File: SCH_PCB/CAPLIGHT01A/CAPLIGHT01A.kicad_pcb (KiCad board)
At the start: 2 copper layers, 59.7 x 20.3 mm, 29 parts, among them J1 JUMP_3X2, J10 JUMP_2x1, J11 JUMP_3X2, J13 CONN_2, J2 CONN1_1, J3 CONN1_1, J4 CONN1_1, J5 CONN1_1, J6 CONN1_1, J7 CONN1_1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

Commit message: nová verze
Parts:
- C3: moved to B.Cu
- moved C3 6.35 mm to (201.9, 121.9)
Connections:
- D2 pad 1: GND -> Net-(C2-Pad2)
- R7 pad 1: Net-(C2-Pad1) -> (no net)
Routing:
- net Net-(C2-Pad2): track 45.1 -> 83.9 mm, vias 0 -> 1
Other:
- board size 59.7 x 20.3 mm -> 73.7 x 20.3 mm

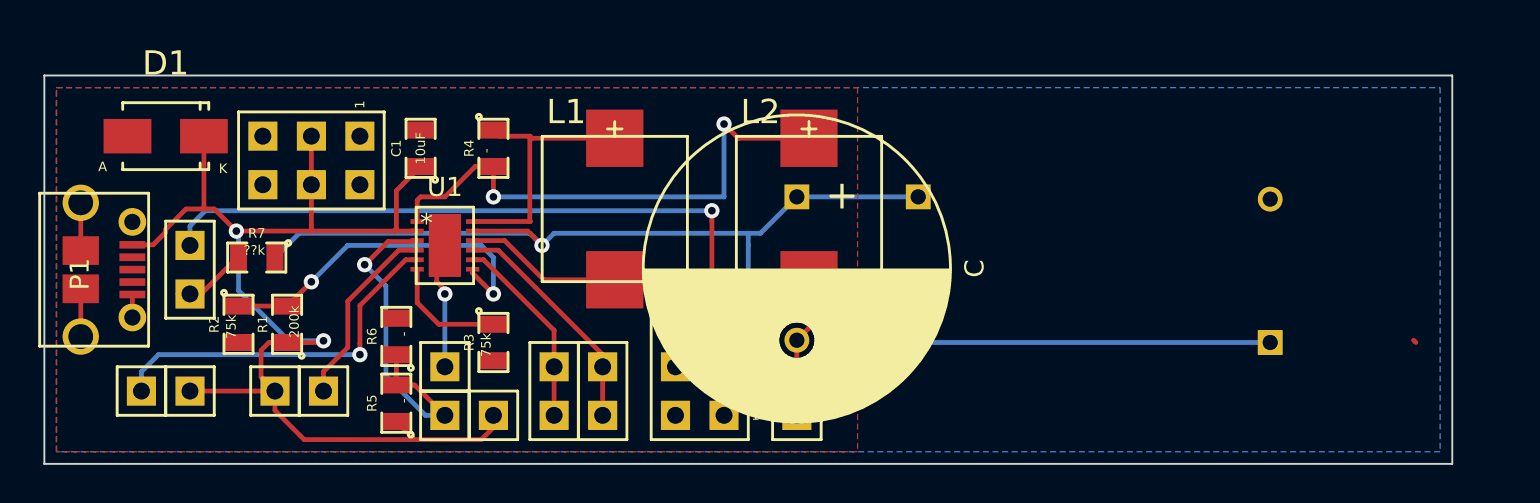
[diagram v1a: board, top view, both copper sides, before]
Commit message: Second capacitor SMD pad
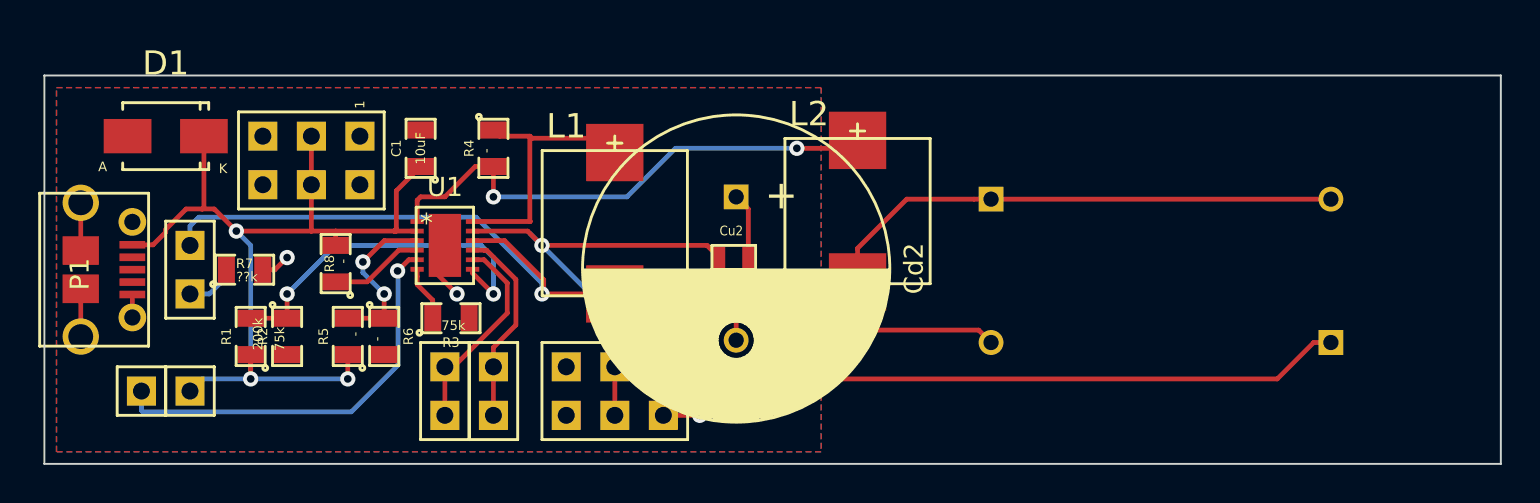
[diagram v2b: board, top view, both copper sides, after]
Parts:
- removed C: C, Mlab_C:C_Radial_D16_L25_P7.5
- removed C2, C3: 22F, Mlab_C:C_Radial_D16_L25_P7.5
- removed J13: CONN_2, Mlab_Pin_Headers:Straight_1x01
- removed J2, J3, J4, J7, J8: CONN1_1, Mlab_Pin_Headers:Straight_1x01
- added Cd1: 22F, Mlab_C:C_Radial_D16_L25_P7.5, B.Cu at (187.3, 114.4)
- added Cd2: 22F, Mlab_C:C_Radial_D16_L25_P7.5, F.Cu at (174.0, 114.3)
- added Cu1: 22F, Mlab_C:C_Radial_D16_L25_P7.5, B.Cu at (205.1, 121.9)
- added Cu2: 100uF, Mlab_C:SMD-0603, F.Cu at (173.9, 117.5)
- added R8: -, Mlab_R:SMD-0805, F.Cu at (153.0, 117.8)
- moved J10 5.72 mm to (161.3, 124.5), turned to 270 degrees
- moved J9 5.72 mm to (158.8, 124.5)
- moved J11 4.62 mm to (167.6, 124.5), turned to 270 degrees
- moved J5 4.45 mm to (145.4, 124.5)
- moved R5 4.32 mm to (153.7, 121.6)
- moved R2 2.62 mm to (150.5, 121.6)
- moved R3 2.56 mm to (159.1, 120.7), turned to 0 degrees
- moved L2 2.54 mm to (180.3, 115.0)
- moved R1 2.01 mm to (148.6, 121.6)
- moved R7 0.90 mm to (148.3, 118.1), turned to 0 degrees
- moved L1 0.75 mm to (167.6, 115.7)
- moved R6 0.64 mm to (155.6, 121.6), turned to 270 degrees
- turned D2 to 180 degrees
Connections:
- net /CTL renamed Net-(R5-Pad2)
- D2 pad 1: Net-(C2-Pad2) -> Net-(D2-Pad1)
- D2 pad 2: Net-(D2-Pad2) -> Net-(Cd1-Pad1)
- L1 pad 2: Net-(C2-Pad2) -> Net-(Cd1-Pad1)
- L2 pad 2: Net-(C2-Pad2) -> Net-(Cd1-Pad1)
- R7 pad 1: (no net) -> Net-(D2-Pad1)
- R7 pad 2: Net-(D2-Pad2) -> GND
- U1 pad 10: Net-(C2-Pad2) -> Net-(Cd1-Pad1)
- U1 pad 4: /VSEL -> Net-(R8-Pad1)
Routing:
- net Net-(C2-Pad2): track 83.9 -> 0.00 mm, vias 1 -> 0
- net Net-(Cd1-Pad1): track 0.00 -> 76.0 mm, vias 0 -> 1
- net GND: track 11.9 -> 29.8 mm, vias 1 -> 7
- net Net-(Cu1-Pad1): track 50.2 -> 65.7 mm, vias 1 -> 2
- net /VIN: track 63.8 -> 49.0 mm, vias 2 -> 3
- net /VSEL: track 9.96 -> 0.00 mm
- net Net-(R5-Pad2): track 18.5 -> 8.82 mm, vias 1 -> 2
- net Net-(R8-Pad1): track 0.00 -> 4.95 mm
- net Net-(R3-Pad1): track 6.84 -> 2.90 mm
- net Net-(D2-Pad2): track 3.83 -> 0.00 mm
- net Net-(D2-Pad1): track 0.00 -> 2.65 mm
- net /EN: track 19.4 -> 21.7 mm
- net /PG: track 12.2 -> 10.5 mm
- net /#PFO: track 10.2 -> 10.9 mm
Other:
- board size 73.7 x 20.3 mm -> 76.2 x 20.3 mm
- board text added: "#PFO"
- board text added: "EN"
- board text added: "PG"
- board text added: "VIN"
- board text added: "VOUT"

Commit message: pcb labels
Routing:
- net Net-(Cu1-Pad1): track 65.7 -> 64.7 mm
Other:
- net class Default: trace_width 0.25 -> 0.3
- rule via_min_size: 0.4 -> 0.7
- board text added: "LED"
- board text added: "OUT"
- board text added: "Power IN"
- board text removed: "VIN"
- board text removed: "VOUT"

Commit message: label
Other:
- board text added: "+"
- board text added: "2016"
- board text added: "CAPLIGHT01A"
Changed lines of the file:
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@@
   (general
     (links 66)
-    (no_connects 1)
-    (area 131.754999 86.207271 215.4975 131.135002)
+    (no_connects 0)
+    (area 137.744999 107.899999 214.045001 128.320001)
     (thickness 1.6)
-    (drawings 13)
-    (tracks 168)
+    (drawings 16)
+    (tracks 169)
     (zones 0)
     (modules 25)
@@
     )
   )
+  (gr_text + (at 176.53 114.3) (layer B.SilkS)
+    (effects (font (size 2 2) (thickness 0.3)) (justify mirror))
+  )
+  (gr_text 2016 (at 167.005 111.76) (layer B.SilkS)
+    (effects (font (size 1.3 1.3) (thickness 0.3)) (justify mirror))
+  )
+  (gr_text CAPLIGHT01A (at 167.64 109.855) (layer B.SilkS)
+    (effects (font (size 1.5 1.5) (thickness 0.35)) (justify mirror))
+  )
   (gr_line (start 178.435 107.95) (end 178.435 128.27) (layer B.SilkS) (width 0.2))
   (gr_text LED (at 148.59 118.11) (layer B.SilkS)
@@
     (effects (font (size 1.5 1.5) (thickness 0.3)) (justify mirror))
   )
-  (gr_text "Power IN\n" (at 151.765 109.22) (layer B.SilkS)
+  (gr_text "Power IN\n" (at 150.495 109.22) (layer B.SilkS)
     (effects (font (size 1.5 1.5) (thickness 0.3)) (justify mirror))
   )
@@
   (segment (start 157.3 118.8865) (end 157.3 118.465) (width 0.25) (layer F.Cu) (net 9))
   (segment (start 157.3 118.465) (end 157.3 118.09) (width 0.25) (layer F.Cu) (net 9))
-  (segment (start 147.32 118.487) (end 147.32 118.11) (width 0.25) (layer B.Cu) (net 10))
-  (segment (start 145.415 119.38) (end 146.427 119.38) (width 0.25) (layer B.Cu) (net 10))
-  (segment (start 146.427 119.38) (end 147.32 118.487) (width 0.25) (layer B.Cu) (net 10))
+  (segment (start 146.05 118.745) (end 146.05 118.6355) (width 0.3) (layer F.Cu) (net 10))
+  (segment (start 146.05 118.6355) (end 146.5755 118.11) (width 0.3) (layer F.Cu) (net 10))
+  (segment (start 146.5755 118.11) (end 147.32 118.11) (width 0.3) (layer F.Cu) (net 10))
+  (segment (start 145.415 119.38) (end 146.05 118.745) (width 0.3) (layer F.Cu) (net 10))
   (segment (start 187.325 114.42) (end 205.105 114.42) (width 0.25) (layer F.Cu) (net 11))
   (segment (start 180.34 118.745) (end 180.34 116.995) (width 0.25) (layer F.Cu) (net 11))

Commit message: only for ExpaLight
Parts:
- removed Cd1, Cd2, Cu1: 22F, Mlab_C:C_Radial_D16_L25_P7.5
- removed Cu2: 100uF, Mlab_C:SMD-0603
- removed J10, J9: JUMP_2x1, Mlab_Pin_Headers:Straight_2x01
- removed J11: JUMP_3X2, Mlab_Pin_Headers:Straight_2x03
- removed J5, J6: CONN1_1, Mlab_Pin_Headers:Straight_1x01
- removed L2: DER0705-3.3uH, Mlab_L:DER0705
- removed R6, R8: -, Mlab_R:SMD-0805
- removed R7: ??k, Mlab_R:SMD-0805
- added C2: 100uF, Mlab_C:TantalC_SizeC_Reflow, F.Cu at (156.9, 123.2)
- added C3: 22F, Mlab_C:C_Radial_D18_L25_P7.5, B.Cu at (168.3, 121.8)
- added J2: CONN1_1, Mlab_Pin_Headers:Straight_1x01, F.Cu at (150.5, 109.9)
- added J3: CONN1_1, Mlab_Pin_Headers:Straight_1x01, F.Cu at (150.5, 112.4)
- R1: value 200k -> -
- R2: value 75k -> 287k
- R3: value 75k -> 100k
- R4: value - -> 71.5k
- R5: value - -> ??k
- moved D1 14.1 mm to (142.3, 125.1)
- moved R1 11.4 mm to (153.7, 111.4)
- moved R4 11.1 mm to (150.8, 115.6), turned to 180 degrees
- moved R3 8.86 mm to (150.5, 118.4), turned to 90 degrees
- moved J1 7.10 mm to (144.8, 111.1), turned to 90 degrees
- moved R5 6.84 mm to (147.3, 124.1)
- moved L1 5.08 mm to (162.6, 115.7)
- moved U1 3.85 mm to (154.9, 117.0), turned to 270 degrees
- moved C1 1.31 mm to (156.2, 111.4), turned to 270 degrees
- moved D2 1.27 mm to (146.7, 118.1), turned to 0 degrees
- moved R2 0.63 mm to (150.5, 122.2), turned to 90 degrees
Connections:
- D2 pad 1: Net-(D2-Pad1) -> GND
- D2 pad 2: Net-(Cd1-Pad1) -> Net-(D2-Pad2)
- L1 pad 2: Net-(Cd1-Pad1) -> Net-(C2-Pad2)
- R1 pad 1: /VIN -> Net-(R1-Pad1)
- R1 pad 2: Net-(R1-Pad2) -> /VIN
- R2 pad 1: Net-(R1-Pad2) -> /VIN
- R2 pad 2: GND -> Net-(R2-Pad2)
- R3 pad 1: Net-(R3-Pad1) -> Net-(R2-Pad2)
- R4 pad 1: Net-(L1-Pad1) -> Net-(R4-Pad1)
- R4 pad 2: Net-(L2-Pad1) -> GND
- R5 pad 1: /VIN -> Net-(C2-Pad2)
- R5 pad 2: Net-(R5-Pad2) -> Net-(D2-Pad2)
- U1 pad 1: Net-(L2-Pad1) -> Net-(L1-Pad1)
- U1 pad 10: Net-(Cd1-Pad1) -> Net-(C2-Pad2)
- U1 pad 3: Net-(R5-Pad2) -> /VIN
- U1 pad 4: Net-(R8-Pad1) -> Net-(R1-Pad1)
- U1 pad 6: Net-(R3-Pad1) -> Net-(R4-Pad1)
- U1 pad 7: Net-(R1-Pad2) -> Net-(R2-Pad2)
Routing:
- net Net-(Cd1-Pad1): track 76.0 -> 0.00 mm, vias 1 -> 0
- net Net-(C2-Pad1): track 64.7 -> 6.25 mm, vias 2 -> 0
- net Net-(C2-Pad2): track 0.00 -> 33.0 mm
- net GND: track 29.8 -> 0.00 mm, vias 7 -> 5
- net Net-(L2-Pad1): track 27.7 -> 0.00 mm, vias 2 -> 0
- net Net-(R1-Pad2): track 18.9 -> 0.00 mm, vias 2 -> 0
- net /EN: track 21.7 -> 6.48 mm, vias 1 -> 0
- net /#PFO: track 10.9 -> 0.00 mm
- net /PG: track 10.5 -> 0.00 mm
- net Net-(R5-Pad2): track 8.82 -> 0.00 mm, vias 2 -> 0
- net Net-(R2-Pad2): track 0.00 -> 5.43 mm
- net Net-(R8-Pad1): track 4.95 -> 0.00 mm
- net Net-(D2-Pad2): track 0.00 -> 4.07 mm
- net Net-(R1-Pad1): track 0.00 -> 3.61 mm
- net Net-(R3-Pad1): track 2.90 -> 0.00 mm
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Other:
- board size 76.2 x 20.3 mm -> 33 x 20.3 mm
- board text removed: "#PFO"
- board text removed: "+"
- board text removed: "2016"
- board text removed: "CAPLIGHT01A"
- board text removed: "EN"
- board text removed: "LED"
- board text removed: "OUT"
- board text removed: "PG"
- board text removed: "Power IN"

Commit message: layout edit
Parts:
- J2: footprint Mlab_Pin_Headers:Straight_1x01 -> Measurement_Points:Measurement_Point_Round-SMD-Pad_Small
- J3: value CONN1_1 -> JUMP_2x1; footprint Mlab_Pin_Headers:Straight_1x01 -> Measurement_Points:Measurement_Point_Round-SMD-Pad_Small
- moved J3 8.64 mm to (153.0, 120.7), turned to 0 degrees
- moved J2 2.54 mm to (150.5, 112.4)
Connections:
- J2 pad 1: /VIN -> /EN
- J3 pad 1: /EN -> /#PFO
- U1 pad 9: /PG -> (no net)
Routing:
- net GND: track 0.00 -> 7.32 mm, vias 5 -> 0
- net Net-(L1-Pad1): track 11.9 -> 17.6 mm, vias 0 -> 4
- net /#PFO: track 0.00 -> 2.81 mm
- net /VIN: track 47.0 -> 45.4 mm
- net /EN: track 6.48 -> 5.37 mm
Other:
- board text added: "CAPLIGHT01A 2016"
- board text added: "POWER IN"

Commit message: tracks width
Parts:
- moved C1 0.51 mm to (156.7, 111.4), turned to 90 degrees
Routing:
- net Net-(C2-Pad2): track 33.0 -> 35.1 mm
- net Net-(L1-Pad1): track 17.6 -> 15.9 mm, vias 4 -> 2
- net GND: track 7.32 -> 7.35 mm, vias 0 -> 8
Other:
- net class Default: clearance 0.2 -> 0.15
- net class thick added: clearance 0.2, trace_width 0.3, via_dia 0.8, via_drill 0.4
- rule trace_clearance: 0.2 -> 0.15
- board text added: "+"
- board text added: "CAPLIGHT01A"
- board text added: "LED"
- board text removed: "CAPLIGHT01A 2016"

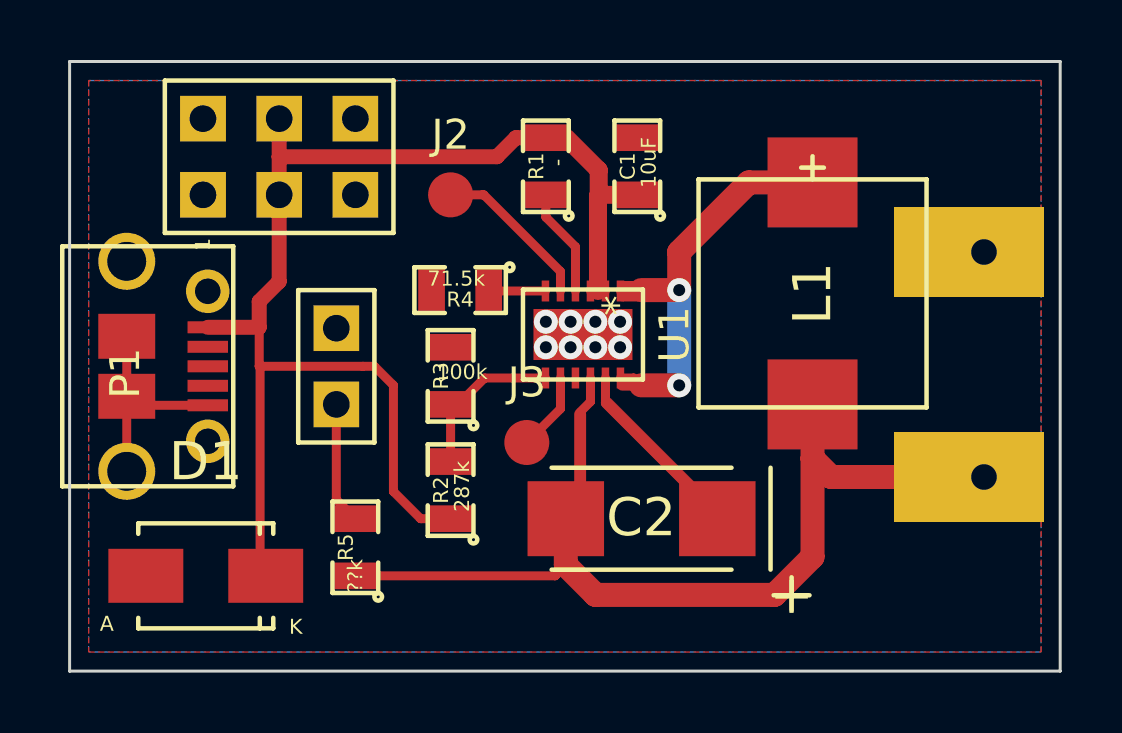
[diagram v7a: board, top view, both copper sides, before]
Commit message: New charge indicating LED added. Manufacturing files generated.
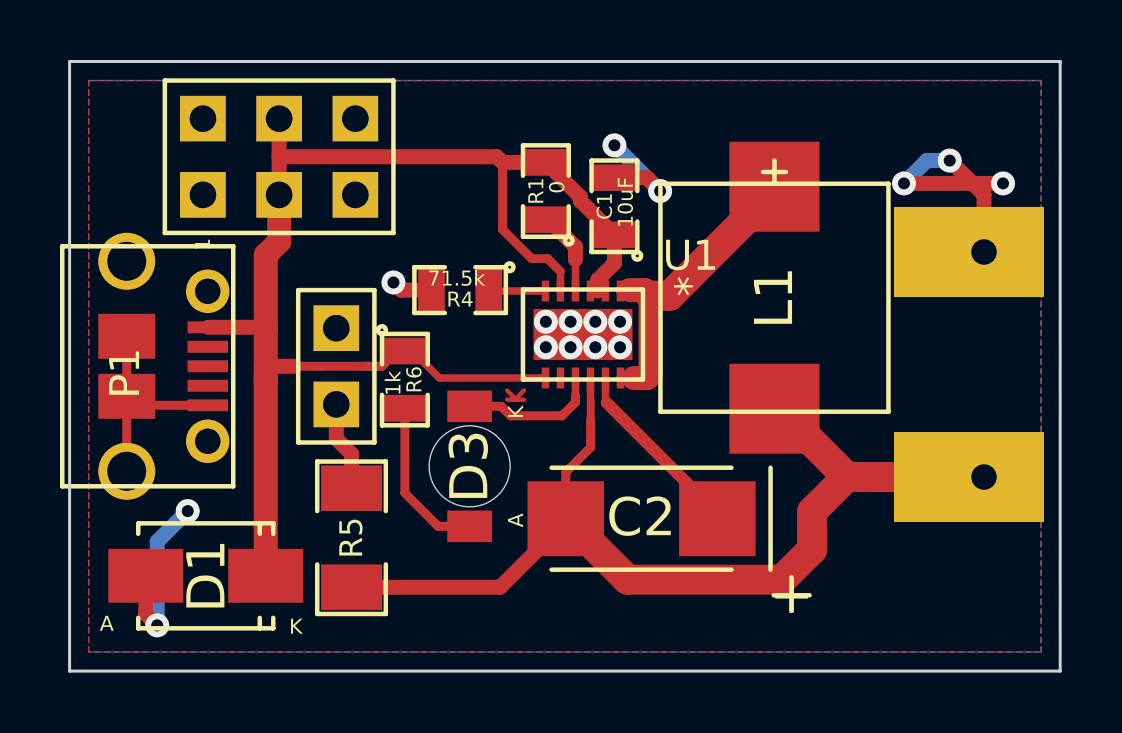
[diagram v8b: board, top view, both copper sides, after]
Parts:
- removed J2: CONN1_1, Measurement_Points:Measurement_Point_Round-SMD-Pad_Small
- removed J3: JUMP_2x1, Measurement_Points:Measurement_Point_Round-SMD-Pad_Small
- removed R2: 287k, Mlab_R:SMD-0805
- removed R3: 100k, Mlab_R:SMD-0805
- added D3: LED, Mlab_D:LED_1206, F.Cu at (151.1, 121.4)
- added R6: 1k, Mlab_R:SMD-0805, F.Cu at (149.0, 118.6)
- C3: value 22F -> 50F
- R1: value - -> 0
- R5: value ??k -> 1k; footprint Mlab_R:SMD-0805 -> Mlab_R:SMD-1206
- moved C1 1.54 mm to (156.0, 112.8)
- moved L1 1.28 mm to (161.3, 115.8)
- moved R1 0.83 mm to (153.7, 112.3)
- moved R5 0.34 mm to (147.2, 123.8)
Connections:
- U1 pad 5: /EN -> /VIN
- U1 pad 7: Net-(R2-Pad2) -> /VIN
- U1 pad 8: /#PFO -> (no net)
- U1 pad 9: (no net) -> /PG
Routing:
- net GND: track 7.35 -> 27.3 mm, vias 8 -> 16
- net Net-(C2-Pad2): track 35.1 -> 40.6 mm
- net Net-(D3-Pad2): track 0.00 -> 5.45 mm
- net Net-(R2-Pad2): track 5.43 -> 0.00 mm
- net /EN: track 5.37 -> 0.00 mm
- net Net-(L1-Pad1): track 15.9 -> 10.8 mm, vias 2 -> 0
- net /PG: track 0.00 -> 4.93 mm
- net /VIN: track 45.2 -> 49.3 mm
- net /#PFO: track 2.61 -> 0.00 mm
- net Net-(D2-Pad2): track 4.07 -> 3.00 mm
- net Net-(R1-Pad1): track 3.61 -> 2.84 mm
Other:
- net class Default: clearance 0.15 -> 0.2
- net class thick: trace_width 0.3 -> 0.8
- rule trace_clearance: 0.15 -> 0.2
- rule trace_min: 0.2 -> 0.25
- board text added: "Charging"
- board text added: "IN"
- board text added: "UST.cz"
- board text removed: "POWER IN"
